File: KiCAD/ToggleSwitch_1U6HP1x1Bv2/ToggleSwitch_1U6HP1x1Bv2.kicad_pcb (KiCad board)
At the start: 2 copper layers, 30 x 39.7 mm, 5 parts, among them SW1 SW_M6/M6.35_Panel_Mount_Hole

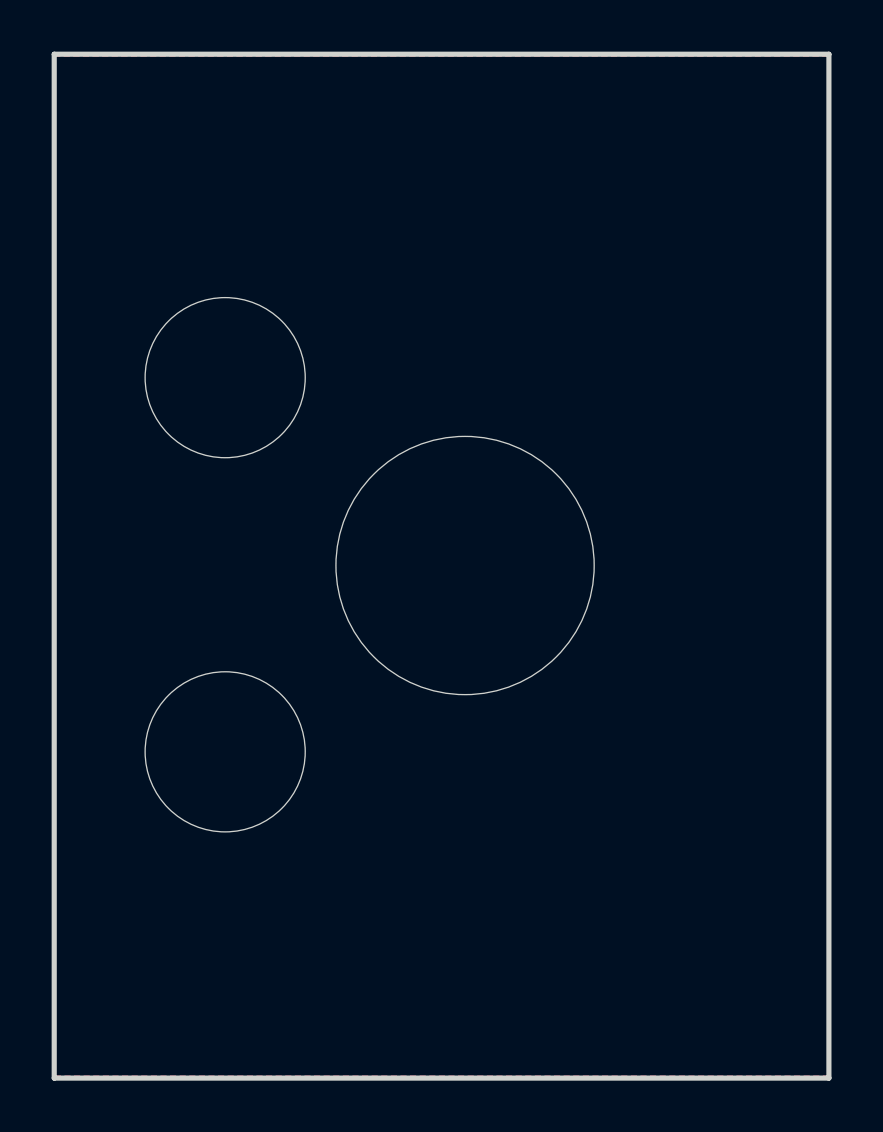
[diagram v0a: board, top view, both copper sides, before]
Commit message: updated all modules to use plated through-holes wherever possible
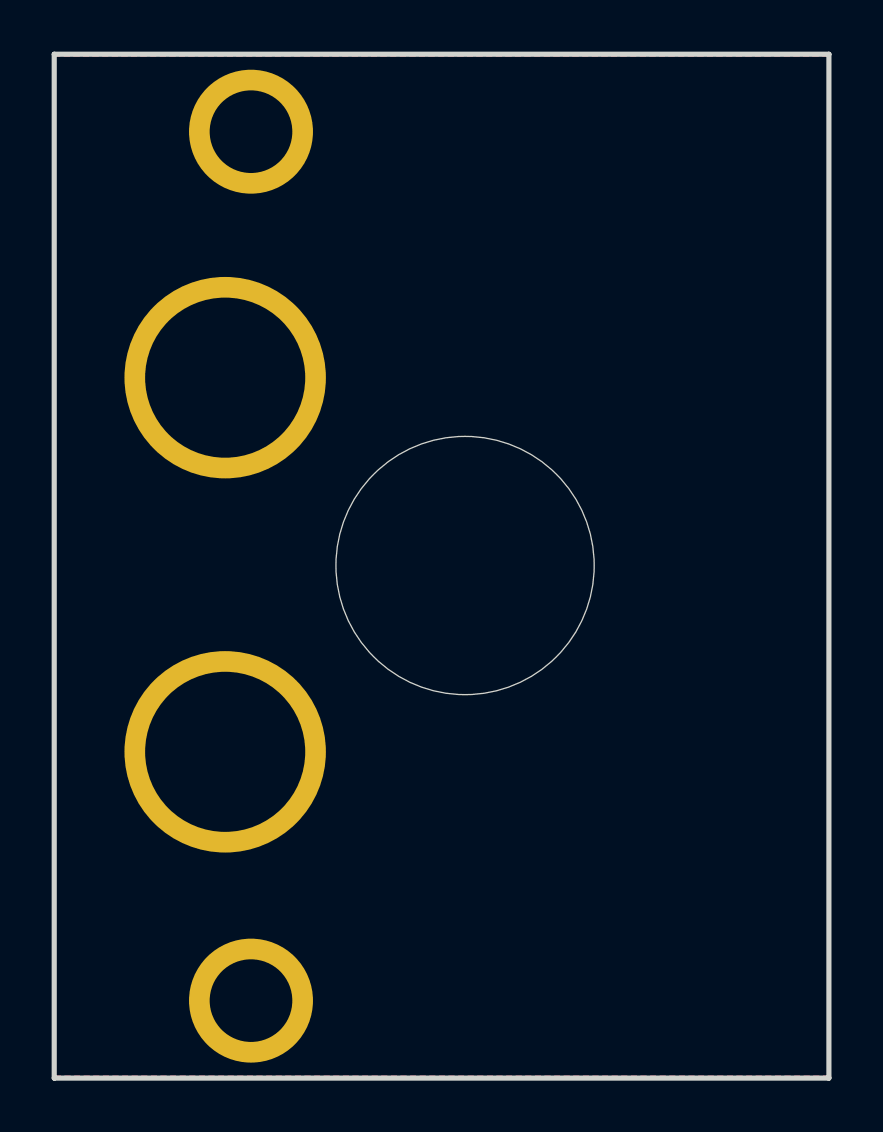
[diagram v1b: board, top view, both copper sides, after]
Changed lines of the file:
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@@
 			)
 		)
-		(pad "" np_thru_hole oval
+		(pad "" thru_hole circle
 			(at 0 0)
-			(size 4.34 3.2)
-			(drill oval 4.34 3.2)
+			(size 4.8 4.8)
+			(drill 3.2)
 			(layers "*.Cu" "*.Mask")
+			(remove_unused_layers no)
 		)
 		(embedded_fonts no)
@@
 			)
 		)
-		(pad "" np_thru_hole oval
+		(pad "" thru_hole circle
 			(at 0 0)
-			(size 4.34 3.2)
-			(drill oval 4.34 3.2)
+			(size 4.8 4.8)
+			(drill 3.2)
 			(layers "*.Cu" "*.Mask")
+			(remove_unused_layers no)
 		)
 		(embedded_fonts no)
@@
 			)
 		)
-		(pad "" np_thru_hole circle
+		(pad "" thru_hole circle
 			(at 0 0)
-			(size 6.2 6.2)
+			(size 7.8 7.8)
 			(drill 6.2)
 			(layers "*.Cu" "*.Mask")
+			(remove_unused_layers no)
 		)
 		(embedded_fonts no)
@@
 			)
 		)
-		(pad "" np_thru_hole circle
+		(pad "" thru_hole circle
 			(at 0 0)
-			(size 6.2 6.2)
+			(size 7.8 7.8)
 			(drill 6.2)
 			(layers "*.Cu" "*.Mask")
+			(remove_unused_layers no)
 		)
 		(embedded_fonts no)
